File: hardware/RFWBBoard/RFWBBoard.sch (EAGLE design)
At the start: 61 parts, among them IC1 24LC025ST, J1 CON-71742-2184-BOT, M1 MOUNT-HOLE3.3, M2 MOUNT-HOLE3.3, M3 MOUNT-HOLE3.3, M4 MOUNT-HOLE3.3, U1 MAX2830IPC-7351, U2 LDB212G4010C-001, U3 LDB212G4010C-001, U4 MAX2830IPC-7351, U5 LDB212G4010C-001, U6 LDB212G4010C-001, X1 LTI-SASF54GT, X2 LTI-SASF54GT, X3 LTI-SASF54GT, X4 LTI-SASF54GT

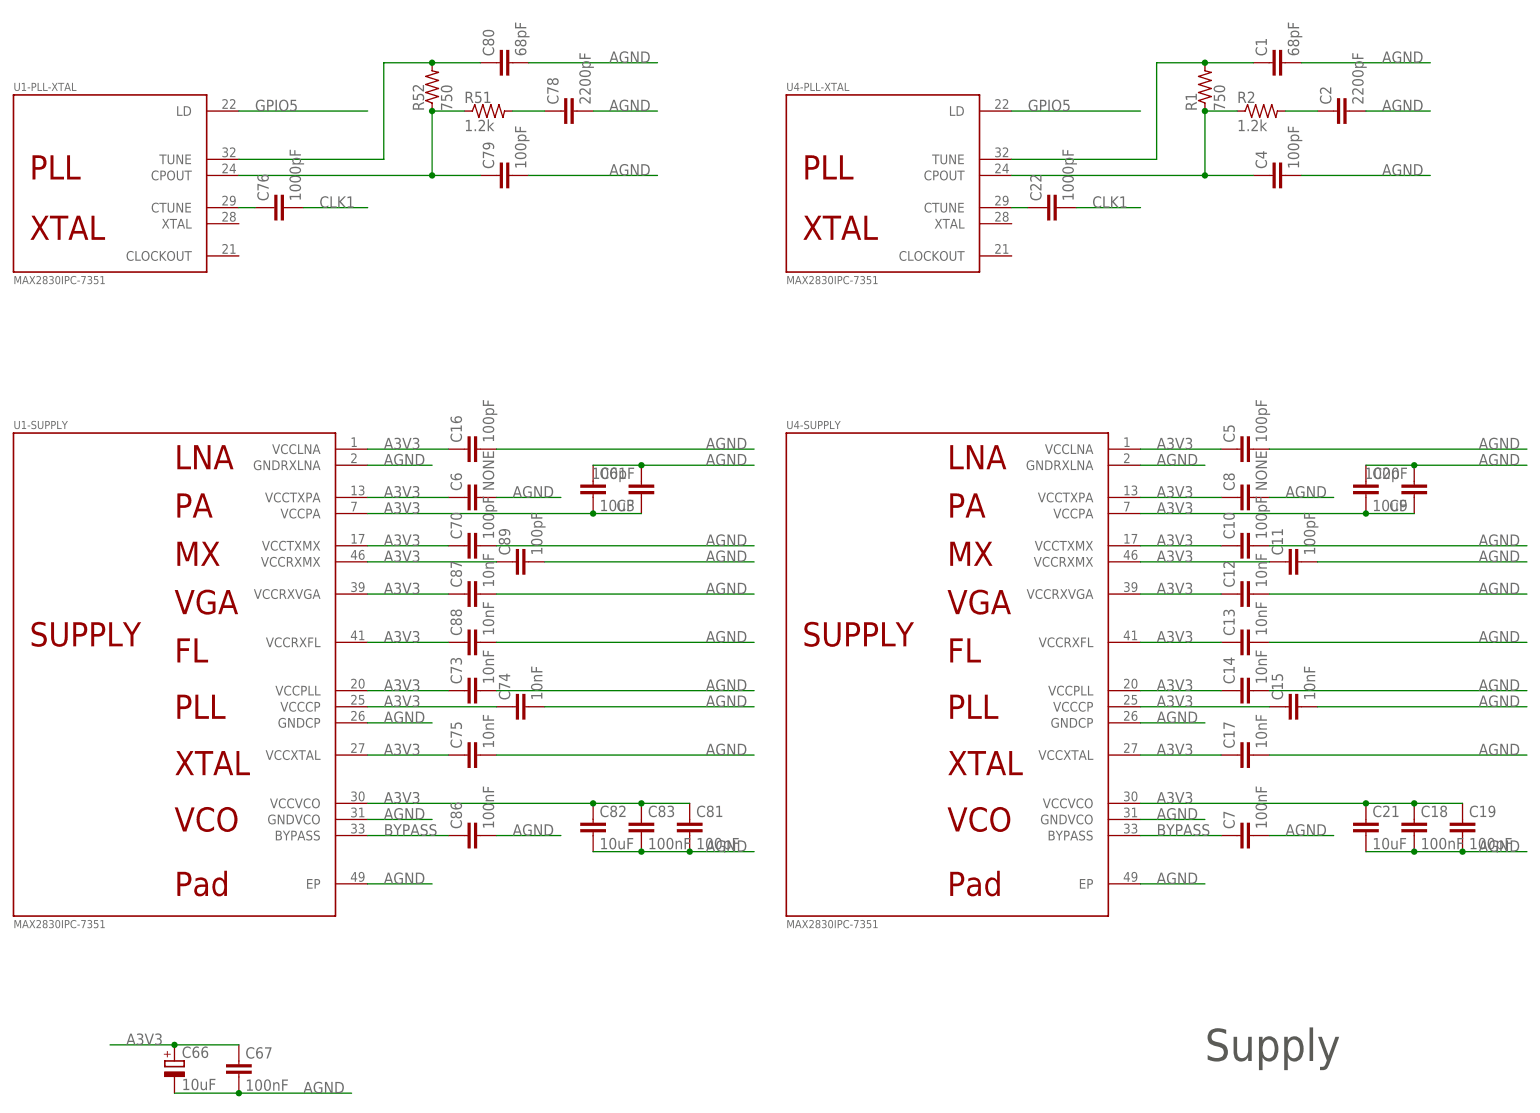
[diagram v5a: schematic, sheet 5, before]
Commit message: - Wide Band RF board routing with DRC check
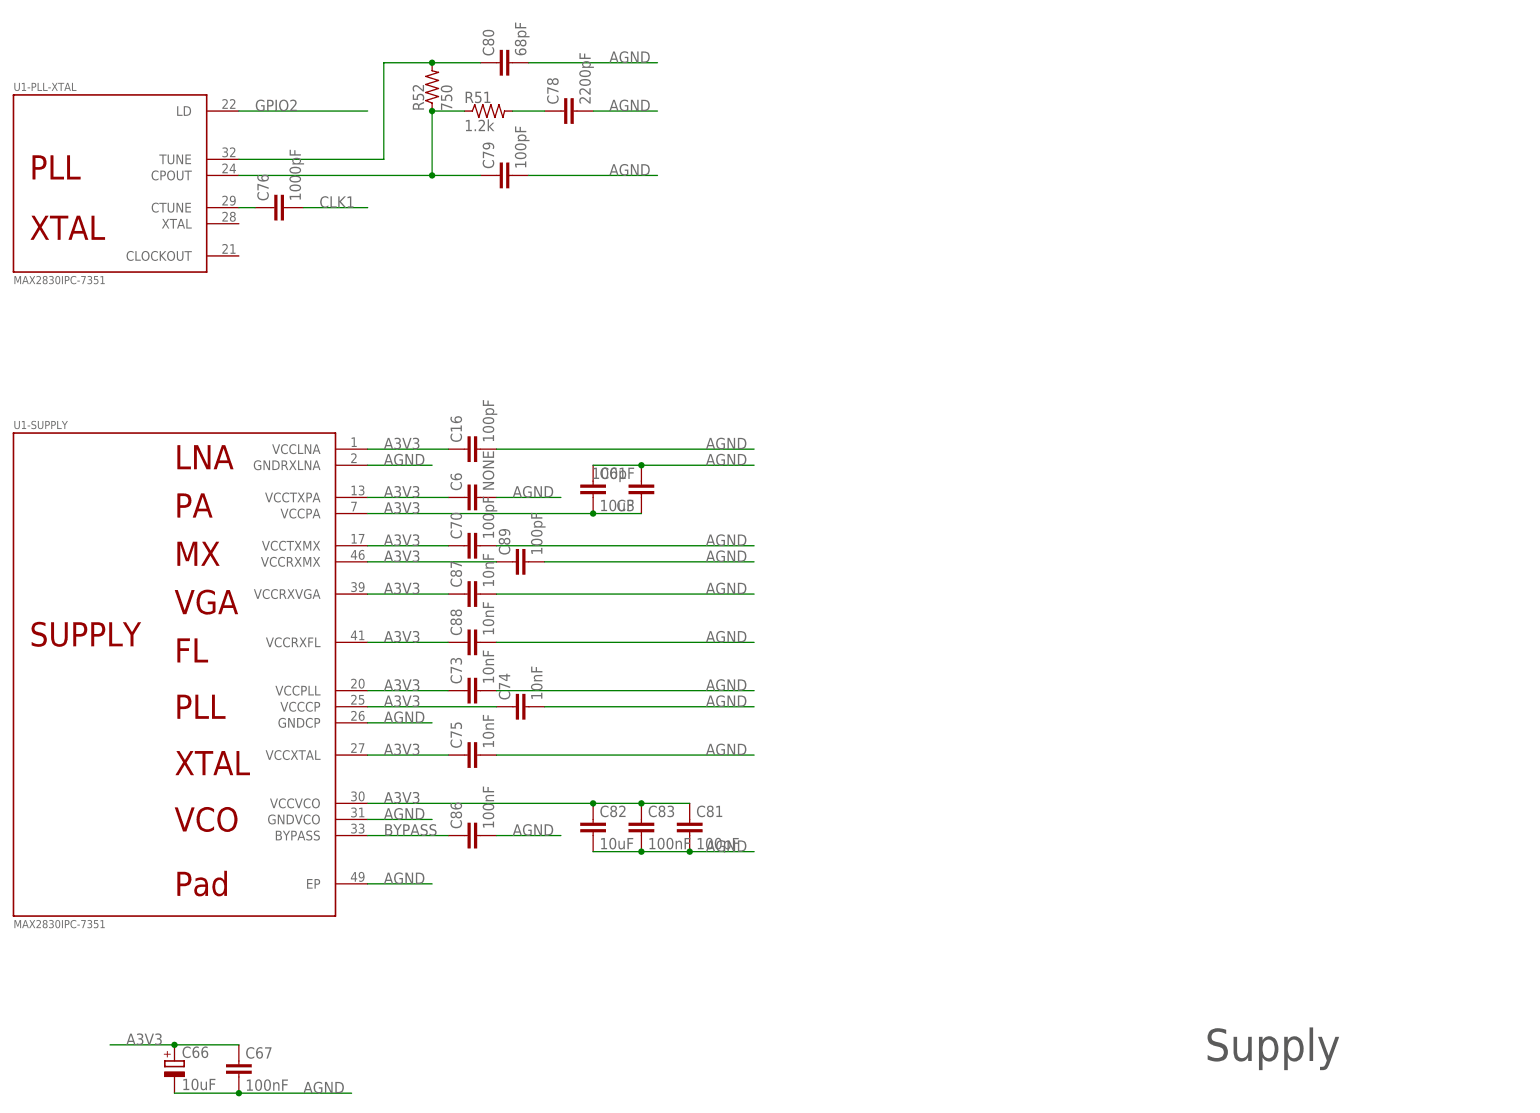
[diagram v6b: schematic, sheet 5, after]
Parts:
- removed C1: 68pF, RFWBBoard:C0402
- removed C10, C11, C19, C4, C5, C9: 100pF, RFWBBoard:C0402
- removed C12, C13, C14, C15, C17: 10nF, RFWBBoard:C0402
- removed C18, C7: 100nF, RFWBBoard:C0402
- removed C2: 2200pF, RFWBBoard:C0402
- removed C20: 10uF, RFWBBoard:C1206
- removed C21: 10uF, RFWBBoard:C0805
- removed C22: 1000pF, RFWBBoard:C0402
- removed C8: NONE, RFWBBoard:C0402
- removed R1: 750, RFWBBoard:R0402
- removed R2: 1.2k, RFWBBoard:R0402
- removed U4: MAX2830IPC-7351, RFWBBoard:MAX2830IPC-7351
- removed U5, U6: LDB212G4010C-001, RFWBBoard:LDB212G4010C-001
- removed X3, X4: LTI-SASF54GT, RFWBBoard:LTI-SASF54GT
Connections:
- removed net N$11: C1.1, R1.2, U4-PLL-XTAL.TUNE
- removed net N$12: C2.1, R2.2
- removed net N$13: C4.1, R1.1, R2.1, U4-PLL-XTAL.CPOUT
- removed net N$14: C22.1, U4-PLL-XTAL.CTUNE
- removed net N$15: U4-ANT.ANT1+, U5.4
- removed net N$16: U4-ANT.ANT2-, U6.3
- removed net N$17: U4-ANT.ANT1-, U5.3
- removed net N$18: U4-ANT.ANT2+, U6.4
- removed net N$19: U5.1, X3G$1.1
- removed net N$20: U6.1, X4G$1.1
- net A3V3: no longer C10.1, C11.1, C12.1, C13.1, C14.1, C15.1, C17.1, C18.1, C19.1, C20.2, C21.1, C5.1, C8.1, C9.1, U4-SUPPLY.VCCCP, U4-SUPPLY.VCCLNA, U4-SUPPLY.VCCPA, U4-SUPPLY.VCCPLL, U4-SUPPLY.VCCRXFL, U4-SUPPLY.VCCRXMX, U4-SUPPLY.VCCRXVGA, U4-SUPPLY.VCCTXMX, U4-SUPPLY.VCCTXPA, U4-SUPPLY.VCCVCO, U4-SUPPLY.VCCXTAL
- net ADC1+: no longer U1-RX.RXBBQ+
- net ADC1-: no longer U1-RX.RXBBQ-
- net ADC2+: no longer U1-RX.RXBBI+
- net ADC2-: no longer U1-RX.RXBBI-
- net ADC3+: now also U1-RX.RXBBQ+; no longer U4-RX.RXBBQ+
- net ADC3-: now also U1-RX.RXBBQ-; no longer U4-RX.RXBBQ-
- net ADC4+: now also U1-RX.RXBBI+; no longer U4-RX.RXBBI+
- net ADC4-: now also U1-RX.RXBBI-; no longer U4-RX.RXBBI-
- net ADCSF1: no longer U1-CONTROL.RSSI
- net ADCSF3: now also U1-CONTROL.RSSI; no longer U4-CONTROL.RSSI
- net AGND: no longer C1.2, C10.2, C11.2, C12.2, C13.2, C14.2, C15.2, C17.2, C18.2, C19.2, C2.2, C20.1, C21.2, C4.2, C5.2, C7.2, C8.2, C9.2, U4-SUPPLY.EP, U4-SUPPLY.GNDCP, U4-SUPPLY.GNDRXLNA, U4-SUPPLY.GNDVCO, U5.2, U5.5, U6.2, U6.5, X3G$1.GND, X3G.GND@1, X3G.GND@2, X3G.GND@3, X4G$1.GND, X4G.GND@1, X4G.GND@2, X4G.GND@3
- net BYPASS: no longer C7.1, U4-SUPPLY.BYPASS
- net CLK1: no longer C22.2
- net DAC1+: no longer U1-TX.TXBBQ+
- net DAC1-: no longer U1-TX.TXBBQ-
- net DAC2+: no longer U1-TX.TXBBI+
- net DAC2-: no longer U1-TX.TXBBI-
- net DAC3+: now also U1-TX.TXBBQ+; no longer U4-TX.TXBBQ+
- net DAC3-: now also U1-TX.TXBBQ-; no longer U4-TX.TXBBQ-
- net DAC4+: now also U1-TX.TXBBI+; no longer U4-TX.TXBBI+
- net DAC4-: now also U1-TX.TXBBI-; no longer U4-TX.TXBBI-
- net GPIO2: now also U1-PLL-XTAL.LD; no longer U1-CONTROL.RXTX
- net GPIO3: now also U1-CONTROL.RXTX; no longer U1-CONTROL.ANTSEL
- net GPIO4: now also U1-CONTROL.ANTSEL; no longer U1-CONTROL.RXHP
- net GPIO5: now also U1-CONTROL.RXHP; no longer U1-PLL-XTAL.LD, U4-PLL-XTAL.LD

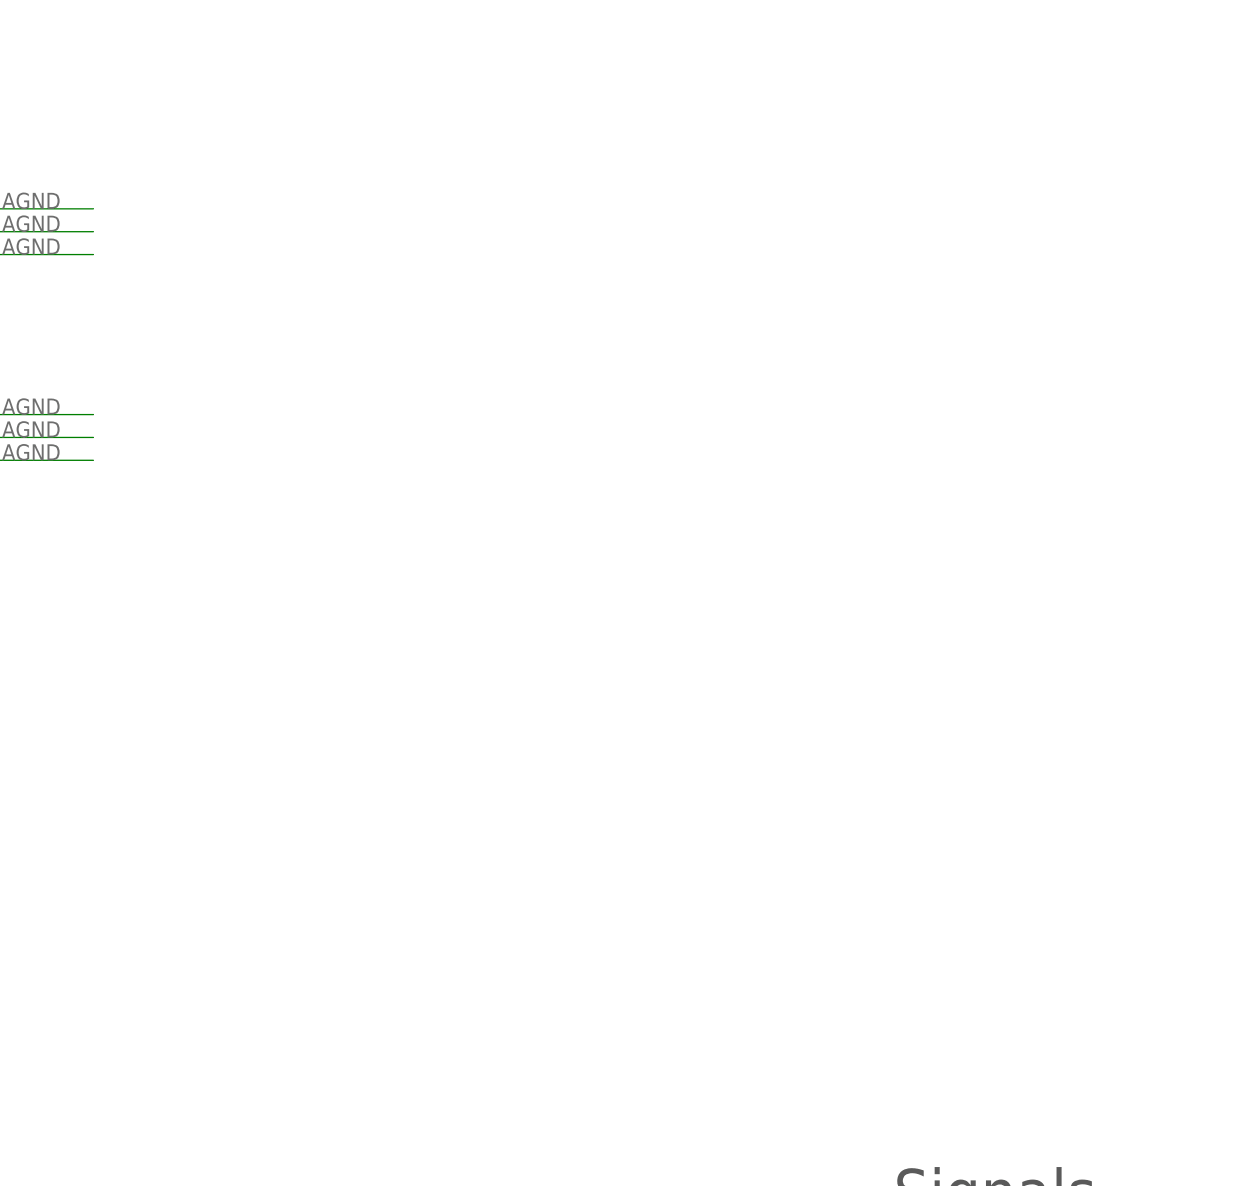
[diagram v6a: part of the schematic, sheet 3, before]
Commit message: - Second MAX2830 removed from RFWBboard - Baseband connections added with AD8132
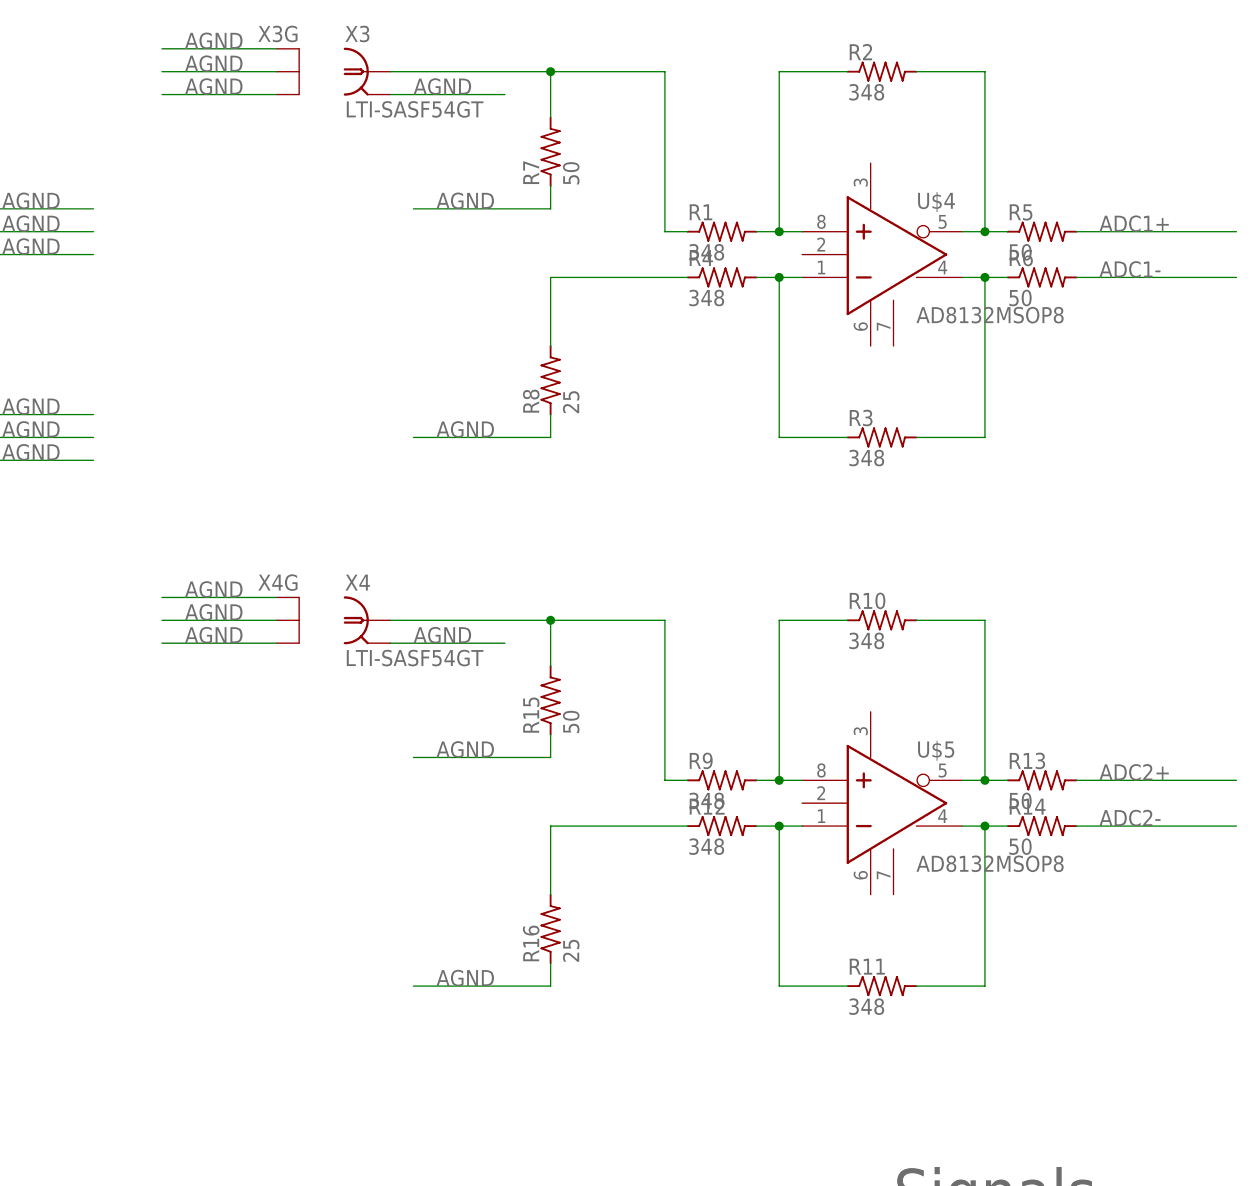
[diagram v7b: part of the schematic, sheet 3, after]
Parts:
- added R1, R10, R11, R12, R2, R3, R4, R9: 348, RFWBBoard:R0402
- added R13, R14, R15, R5, R6, R7: 50, RFWBBoard:R0402
- added R16, R8: 25, RFWBBoard:R0402
- added U$4, U$5: AD8132MSOP8, RFWBBoard:AD8132MSOP8
- added X3, X4: LTI-SASF54GT, RFWBBoard:LTI-SASF54GT
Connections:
- new net N$11: R1.1, R7.2, X3G$1.1
- new net N$12: R2.2, R5.1, U$4.-OUT
- new net N$13: R3.2, R6.1, U$4.+OUT
- new net N$14: R1.2, R2.1, U$4.+IN
- new net N$15: R3.1, R4.2, U$4.-IN
- new net N$16: R15.2, R9.1, X4G$1.1
- new net N$17: R4.1, R8.2
- new net N$18: R10.2, R13.1, U$5.-OUT
- new net N$19: R11.2, R14.1, U$5.+OUT
- new net N$20: R10.1, R9.2, U$5.+IN
- new net N$21: R11.1, R12.2, U$5.-IN
- new net N$22: R12.1, R16.2
- net ADC1+: now also R5.2
- net ADC1-: now also R6.2
- net ADC2+: now also R13.2
- net ADC2-: now also R14.2
- net AGND: now also R15.1, R16.1, R7.1, R8.1, X3G$1.GND, X3G.GND@1, X3G.GND@2, X3G.GND@3, X4G$1.GND, X4G.GND@1, X4G.GND@2, X4G.GND@3
